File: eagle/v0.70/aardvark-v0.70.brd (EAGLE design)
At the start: 25.4 x 76.2 mm, 22 parts, among them IC1 REG1117, X1 MINI-USB-32005-201

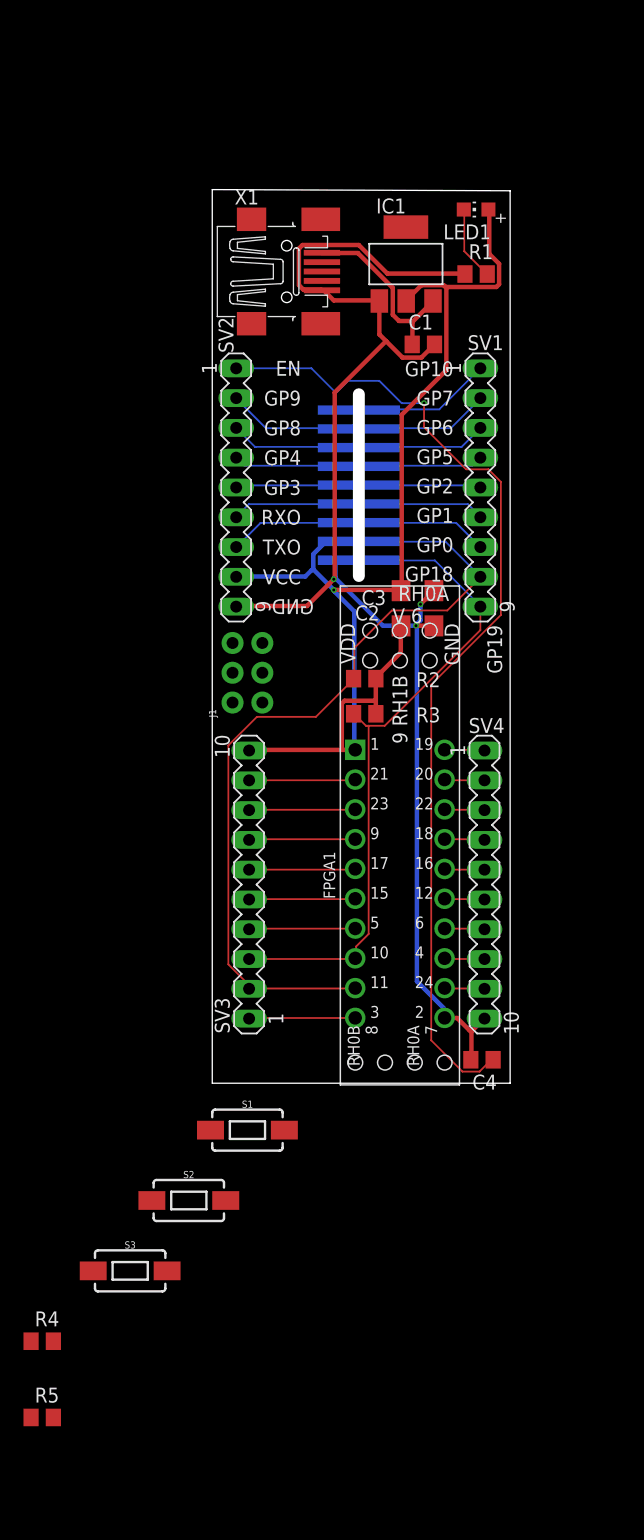
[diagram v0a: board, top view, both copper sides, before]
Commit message: fixed spelling error and mirror image GND designator
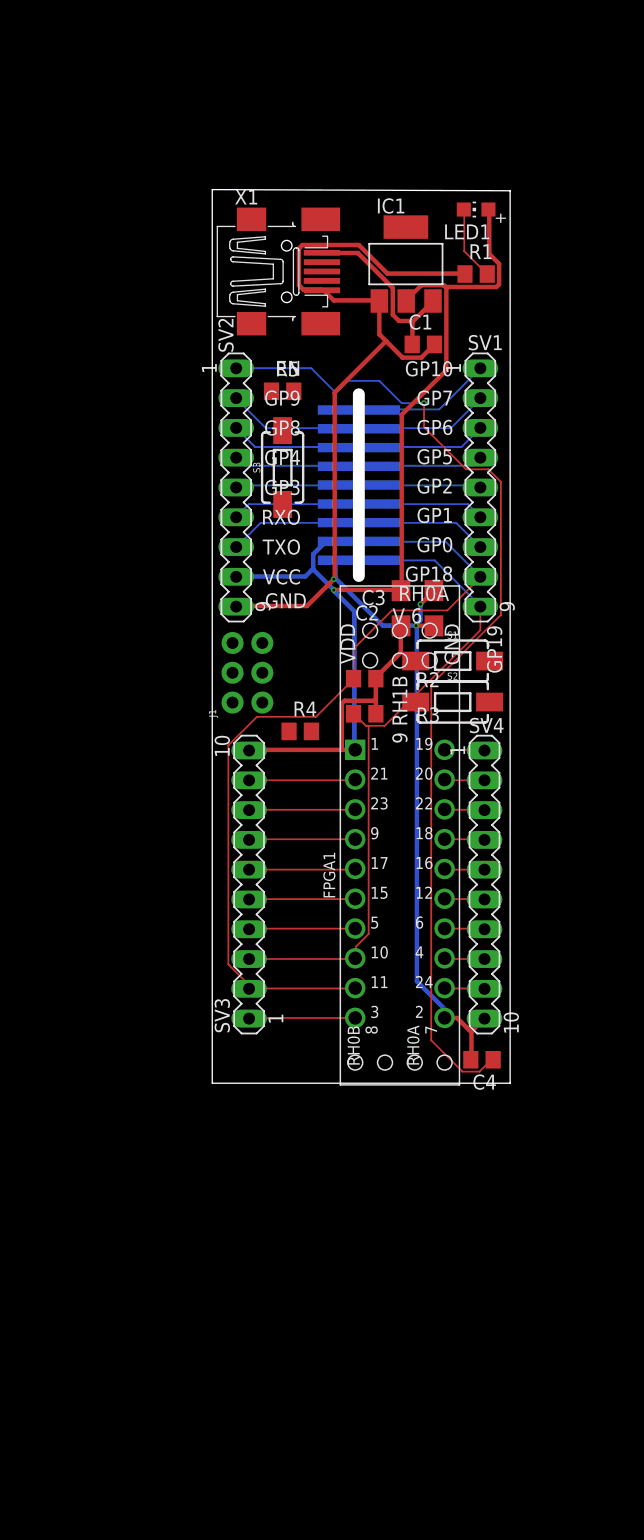
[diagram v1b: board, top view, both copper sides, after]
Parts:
- moved R5 89.9 mm to (6.00, 59.0)
- moved S3 69.7 mm to (6.00, 52.5), turned to 90 degrees
- moved R4 56.5 mm to (7.50, 30.0)
- moved S2 48.1 mm to (20.5, 32.5)
- moved S1 43.7 mm to (20.5, 36.0)
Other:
- board text added: "TriEmbed Community Project Aardvarck 0.70 ESP32-C3 + SLG47004V-DIP"
- board text removed: "TriEmbed Community Project Aardvack 0.70 ESP32-C3 + SLG47004V-DIP"

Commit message: board update: incomplete placement and routing
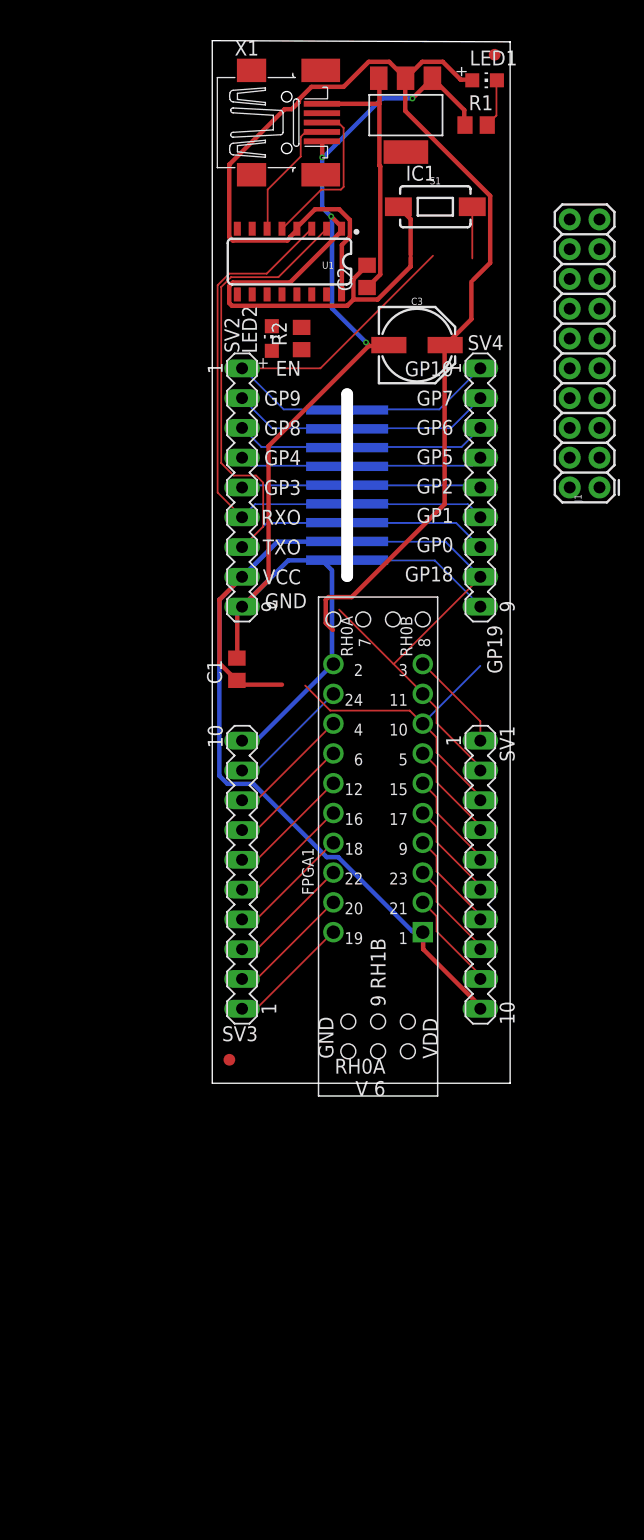
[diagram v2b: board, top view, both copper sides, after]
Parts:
- removed C4: 4.7uF, rcl:C0805
- removed R3: 10K, rcl:R0805
- removed R4, R5: 4.7k, rcl:R0805
- removed S2: BOOT, apexprotofactory:TACTILE_SWITCH_SMD_6.0X3.5MM
- removed S3: VERBOSE, apexprotofactory:TACTILE_SWITCH_SMD_6.0X3.5MM
- removed U$2: UNTITLED_ESP32C3, aardvark-v0.01:UNTITLED_ESP32-C3-01M
- added FD1, FD2: FIDUCIAL1X2, apexprotofactory:FIDUCIAL-1X2
- added LED2: (no value), adafruit:CHIP-LED0805
- added MOD1: (no value), aithinker-C3-M1:ESPRESSIF_ESP32-C3-01M
- added U1: CH340C, SparkFun-IC-Comms:SO016
- C1: value 10uF -> 100nF
- C2: value 68uF -> 10uF; device rcl:C1206 -> rcl:C0805
- C3: value 68uF -> 100uF; device rcl:C1206 -> SparkFun-Capacitors:PANASONIC_D
- FPGA1: value SLG47004V-DIP -> (none); device 22020117-1206PM-SLG47004V-DIP:SLG47004V-DIP -> SLG47004V-DIP:SLG47004V-DIP
- IC1: value REG1117 -> LM1117-3.3
- J1: device SparkFun-Connectors:2X3-NS -> SparkFun-Connectors:2X10
- R2: value 10K -> 510
- S1: value ENABLE -> RESET; device apexprotofactory:TACTILE_SWITCH_SMD_6.0X3.5MM -> SparkFun-Switches:TACTILE_SWITCH_SMD_6.0X3.5MM
- SV1: device con-lstb:MA09-1 -> con-lstb:MA10-1
- SV4: device con-lstb:MA10-1 -> con-lstb:MA09-1
- moved S1 38.8 mm to (19.0, 74.7)
- moved J1 33.9 mm to (33.0, 50.8)
- moved SV4 33.9 mm to (22.9, 50.8)
- moved SV1 33.0 mm to (22.9, 17.8)
- moved C1 31.9 mm to (2.10, 35.3), turned to 90 degrees
- moved C2 30.1 mm to (13.2, 68.8), turned to 90 degrees
- moved R2 29.5 mm to (7.62, 63.5), turned to 90 degrees
- moved C3 20.9 mm to (17.5, 62.9)
- moved IC1 12.7 mm to (16.5, 82.5), turned to 180 degrees
- moved R1 12.7 mm to (22.5, 81.7)
- moved X1 12.7 mm to (6.35, 81.9)
- moved LED1 11.0 mm to (23.2, 85.5), turned to 270 degrees
- moved FPGA1 2.09 mm to (14.1, 18.0), turned to 90 degrees
- moved SV3 1.03 mm to (2.54, 17.8)
- moved SV2 0.50 mm to (2.54, 50.8)
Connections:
- removed net DP4: SV2.4, U$2.PIN4
- removed net GP0: SV1.7, U$2.PIN12
- removed net GP1: SV1.6, U$2.PIN13
- removed net RXO: SV2.6, U$2.PIN6
- new net DTR: U1.13
- new net GP18: MOD1.PIN11, SV4.8
- new net GP19: MOD1.PIN10, SV4.9
- new net GP4: MOD1.PIN4, SV2.4
- new net N$1: LED2.C, R2.2
- new net RTS: U1.14
- new net RXI: MOD1.PIN6, SV2.6, U1.3
- new net UD+: U1.5, X1.3
- new net UD-: U1.6, X1.4
- net EN: now also MOD1.PIN1; no longer C4.1, U$2.PIN1
- net GND: now also C3.-, MOD1.PIN9, R2.1, SV3.10, U1.1; no longer C3.2, C4.2, S2.1, S3.1, SV4.10, U$2.PIN9
- net GP10: now also MOD1.PIN18, SV4.1; no longer SV1.1, U$2.PIN18
- net GP2: now also LED2.A, MOD1.PIN14, SV4.5; no longer SV1.5, U$2.PIN14
- net GP3: now also MOD1.PIN5; no longer U$2.PIN5
- net GP5: now also MOD1.PIN15, SV4.4; no longer SV1.4, U$2.PIN15
- net GP6: now also MOD1.PIN16, SV4.3; no longer SV1.3, U$2.PIN16
- net GP7: now also MOD1.PIN17, SV4.2; no longer SV1.2, U$2.PIN17
- net GP8: now also MOD1.PIN3; no longer R5.2, S3.2, U$2.PIN3
- net GP9: now also MOD1.PIN2; no longer R4.2, S2.2, U$2.PIN2
- net GPI(PIN21): now also SV1.9; no longer SV3.9
- net GPIO(PIN12): now also SV3.6; no longer SV4.6
- net GPIO(PIN15): now also SV1.5; no longer SV3.5
- net GPIO(PIN16): now also SV3.5; no longer SV4.5
- net GPIO(PIN17): now also SV1.6; no longer SV3.6
- net GPIO(PIN18): now also SV3.4; no longer SV4.4
- net GPIO(PIN19): now also SV3.1; no longer SV4.1
- net GPIO(PIN20): now also SV3.2; no longer SV4.2
- net OA0+(PIN4): now also SV3.8; no longer SV4.8
- net OA0-(PIN3): now also SV1.1; no longer SV3.1
- net OA0_OUT(PIN5): now also SV1.4; no longer SV3.4
- net OA1+(PIN23): now also SV1.8; no longer SV3.8
- net OA1-(PIN24): now also SV3.9; no longer SV4.9
- net OA1_OUT(PIN22): now also SV3.3; no longer SV4.3
- net RH0A(PIN6): now also SV3.7; no longer SV4.7
- net RH1B(PIN9): now also SV1.7; no longer SV3.7
- net SCL: now also MOD1.PIN12, SV1.3, SV4.7; no longer R3.1, SV1.9, SV3.3, U$2.PIN10
- net SDA: now also MOD1.PIN13, SV1.2, SV4.6; no longer R2.1, SV1.8, SV3.2, U$2.PIN11
- net TXO: now also MOD1.PIN7, U1.2; no longer U$2.PIN7
- net USBV: now also C2.1; no longer C1.1
- net VCC: now also C1.1, C3.+, MOD1.PIN8, SV1.10, U1.16, U1.4; no longer C2.1, C3.1, R2.2, R3.2, R4.1, R5.1, SV3.10, U$2.PIN8
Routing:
- net VCC: track 100.4 -> 180.0 mm, vias 1 -> 0
- net EN: track 87.0 -> 33.1 mm, vias 1 -> 0
- net RXI: track 0.00 -> 38.1 mm
- net TXO: track 9.32 -> 44.4 mm
- net SDA: track 69.2 -> 39.0 mm
- net SCL: track 56.0 -> 37.1 mm
- net GND: track 122.7 -> 138.0 mm, vias 3 -> 4
- net UD+: track 0.00 -> 13.8 mm
- net GP19: track 0.00 -> 11.0 mm
- net UD-: track 0.00 -> 11.0 mm
- net GP18: track 0.00 -> 10.6 mm
- net GP0: track 9.22 -> 0.00 mm
- net RXO: track 8.94 -> 0.00 mm
- net GP1: track 8.86 -> 0.00 mm
- net DP4: track 8.76 -> 0.00 mm
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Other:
- board size 25.4 x 76.2 mm -> 25.4 x 88.9 mm

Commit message: Fix C3 module footprint, shift pin outside SLG footprint, update notes
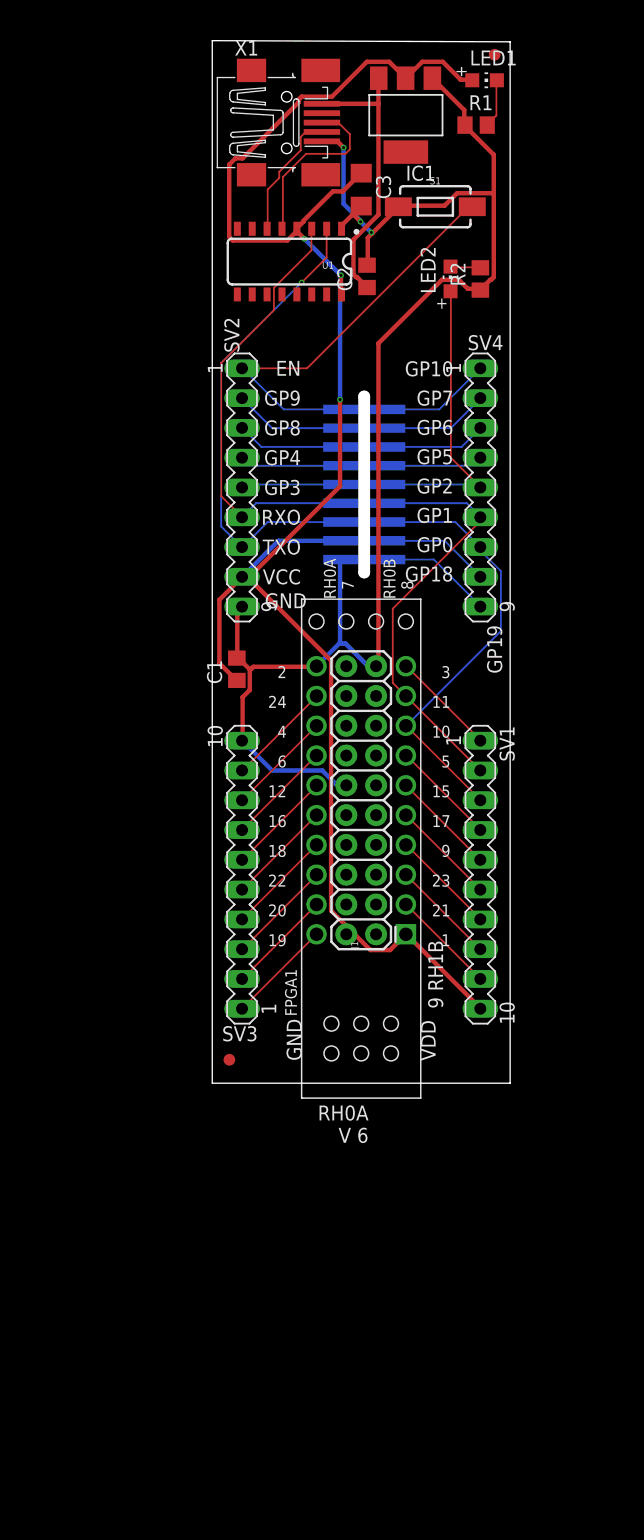
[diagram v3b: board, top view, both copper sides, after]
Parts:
- C3: value 100uF -> (none); device SparkFun-Capacitors:PANASONIC_D -> rcl:C1206
- moved J1 42.6 mm to (14.0, 12.7)
- moved LED2 16.1 mm to (20.3, 68.6)
- moved R2 16.1 mm to (22.9, 68.6)
- moved C3 14.1 mm to (12.7, 76.2), turned to 270 degrees
- moved MOD1 1.46 mm to (13.0, 51.1)
- moved FPGA1 1.45 mm to (12.7, 17.8)
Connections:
- net GND: now also C3.2, J1.12, J1.19; no longer C3.-
- net VCC: now also C3.1, J1.2; no longer C3.+
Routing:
- net VCC: track 180.0 -> 152.7 mm, vias 0 -> 3
- net GP2: track 9.45 -> 25.8 mm
- net GND: track 138.0 -> 130.8 mm, vias 4 -> 3
- net TXO: track 44.4 -> 40.9 mm, vias 0 -> 1
- net SDA: track 39.0 -> 36.2 mm
- net N$1: track 0.00 -> 2.62 mm
- net EN: track 33.1 -> 35.2 mm
- net GPIO(PIN18): track 10.5 -> 8.98 mm
- net GPIO(PIN19): track 10.5 -> 8.98 mm
- net RH0A(PIN6): track 10.5 -> 8.98 mm
- net GP3: track 7.03 -> 8.51 mm
- net GP10: track 10.8 -> 9.36 mm
- net GP7: track 10.5 -> 9.00 mm
- net GP6: track 10.1 -> 8.59 mm
- net GP5: track 9.66 -> 8.19 mm
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
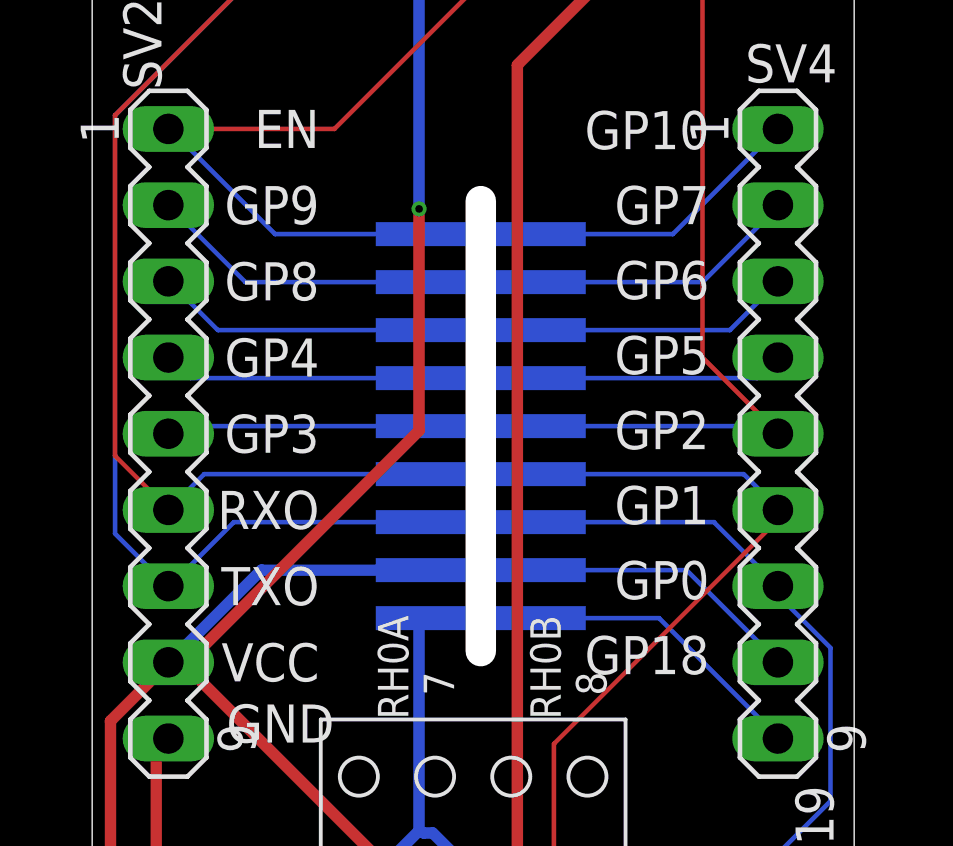
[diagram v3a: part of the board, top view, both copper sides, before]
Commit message: swap C3 board in that really has slot narrowed
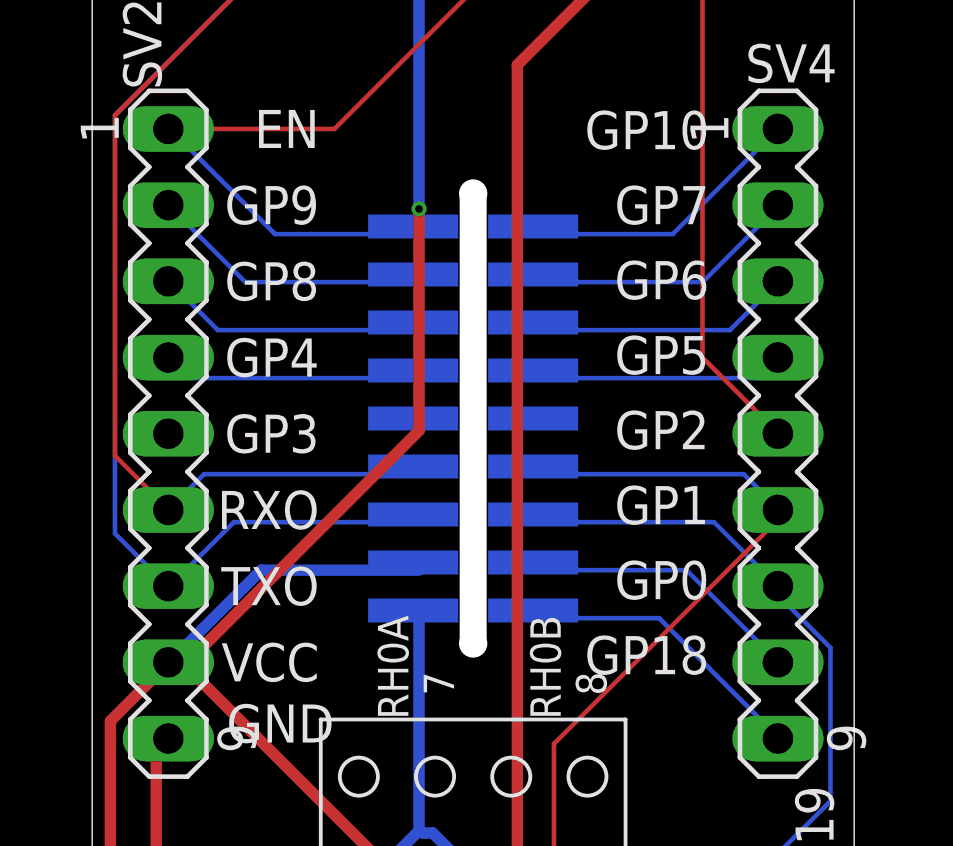
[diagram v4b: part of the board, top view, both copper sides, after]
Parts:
- moved MOD1 0.36 mm to (12.7, 51.3)
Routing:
- net GP3: track 8.51 -> 0.38 mm
- net GP2: track 25.8 -> 18.1 mm

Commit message: added right angle header site for outboard I2C programming
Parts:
- added SV5: (no value), con-lstb:MA04-1
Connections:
- net GND: now also SV5.1
- net SCL: now also SV5.3
- net SDA: now also SV5.4
- net VCC: now also SV5.2
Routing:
- net GND: track 130.8 -> 165.0 mm
- net SDA: track 36.1 -> 65.9 mm
- net SCL: track 37.1 -> 65.6 mm
- net GP2: track 18.1 -> 26.2 mm
- net GP3: track 0.38 -> 8.36 mm
- net VCC: track 152.7 -> 159.8 mm

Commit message: 0.70 release candidate
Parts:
- removed X1: MINI-USB-32005-201, con-cypressindustries:32005-201
- added DIALOG-PGM: (no value), SparkFun-Connectors:2X10
- added LOGO1: OSHW-LOGOMINI, SparkFun-Aesthetics:OSHW-LOGO-MINI
- C1: value 100nF -> 10uF
- C2: value 10uF -> 100uF; device rcl:C0805 -> SparkFun-Capacitors:PANASONIC_D
- C3: value (none) -> 4.7uF; device rcl:C1206 -> rcl:C0805
- FPGA1: value (none) -> SLG47004V-DIP
- J1: value (none) -> USB_MINI-B_SMT; device SparkFun-Connectors:2X10 -> SparkFun-Connectors:USB-MINIB
- LED1, LED2: device adafruit:CHIP-LED0805 -> led:CHIP-LED0805
- MOD1: value (none) -> ESP32-C3-M1; device aithinker-C3-M1:ESPRESSIF_ESP32-C3-01M -> aithinker-C3-M1:AITHINKER-C3-M1
- SV2: device con-lstb:MA09-1 -> con-lstb:MA04-1
- SV3: device con-lstb:MA10-1 -> con-lstb:MA09-1
- SV4: device con-lstb:MA09-1 -> con-lstb:MA10-1
- SV5: device con-lstb:MA04-1 -> con-lstb:MA09-1
- moved J1 70.7 mm to (4.70, 82.8), turned to 0 degrees
- moved SV5 48.6 mm to (22.9, 50.8), turned to 270 degrees
- moved C1 43.9 mm to (12.3, 78.0), turned to 180 degrees
- moved SV4 37.7 mm to (2.54, 19.1), turned to 90 degrees
- moved SV3 33.0 mm to (2.54, 50.8), turned to 270 degrees
- moved C2 16.0 mm to (20.7, 82.9)
- moved LED1 15.7 mm to (13.7, 73.0)
- moved R1 14.8 mm to (13.5, 70.0)
- moved SV2 13.5 mm to (5.17, 64.1), turned to 0 degrees
- moved C3 10.4 mm to (12.4, 65.8)
- moved LED2 6.13 mm to (15.5, 64.8)
- moved R2 5.50 mm to (18.7, 65.0), turned to 270 degrees
- moved IC1 3.55 mm to (13.3, 84.0), turned to 0 degrees
- moved U1 3.21 mm to (5.30, 73.0), turned to 0 degrees
- moved S1 2.50 mm to (20.4, 72.7), turned to 270 degrees
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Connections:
- removed net DTR: U1.13
- removed net RTS: U1.14
- removed net USBV: C2.1, IC1.3, X1.1
- new net VBUS: C1.1, IC1.3, J1.VBUS
- net EN: now also C3.1, SV3.1, U1.14; no longer SV2.1
- net GND: now also C2.-, DIALOG-PGM.12, DIALOG-PGM.19, J1.GND, SV2.1, SV3.9, SV4.10; no longer C2.2, J1.12, J1.19, SV2.9, SV3.10, SV5.1, X1.5
- net GP10: now also SV5.1; no longer SV4.1
- net GP18: now also SV5.8; no longer SV4.8
- net GP19: now also SV5.9; no longer SV4.9
- net GP2: now also SV5.5; no longer SV4.5
- net GP3: now also SV3.5; no longer SV2.5
- net GP4: now also SV3.4; no longer SV2.4
- net GP5: now also SV5.4; no longer SV4.4
- net GP6: now also SV5.3; no longer SV4.3
- net GP7: now also SV5.2; no longer SV4.2
- net GP8: now also SV3.3; no longer SV2.3
- net GP9: now also SV3.2, U1.13; no longer SV2.2
- net GPIO(PIN12): now also SV4.6; no longer SV3.6
- net GPIO(PIN16): now also SV4.5; no longer SV3.5
- net GPIO(PIN18): now also SV4.4; no longer SV3.4
- net GPIO(PIN19): now also SV4.1; no longer SV3.1
- net GPIO(PIN20): now also SV4.2; no longer SV3.2
- net OA0+(PIN4): now also SV4.8; no longer SV3.8
- net OA1-(PIN24): now also SV4.9; no longer SV3.9
- net OA1_OUT(PIN22): now also SV4.3; no longer SV3.3
- net RH0A(PIN6): now also SV4.7; no longer SV3.7
- net RXI: now also SV3.6; no longer SV2.6
- net SCL: now also DIALOG-PGM.8, SV2.3, SV5.7; no longer SV4.7, SV5.3
- net SDA: now also DIALOG-PGM.9, SV2.4, SV5.6; no longer SV4.6, SV5.4
- net TXO: now also SV3.7; no longer SV2.7
- net UD+: now also J1.D+; no longer X1.3
- net UD-: now also J1.D-; no longer X1.4
- net VCC: now also C2.+, DIALOG-PGM.2, SV2.2, SV3.8; no longer C1.1, C3.1, J1.2, SV2.8, SV5.2
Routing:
- net EN: track 34.9 -> 85.6 mm, vias 0 -> 1
- net GND: track 165.0 -> 138.2 mm, vias 3 -> 1
- net VCC: track 159.8 -> 134.7 mm, vias 3 -> 2
- net USBV: track 24.1 -> 0.00 mm
- net GP9: track 9.12 -> 28.2 mm, vias 0 -> 2
- net VBUS: track 0.00 -> 12.6 mm, vias 0 -> 2
- net SDA: track 65.9 -> 77.4 mm
- net SCL: track 65.6 -> 75.5 mm
- net TXO: track 40.8 -> 34.5 mm
- net RXI: track 37.3 -> 31.6 mm, vias 0 -> 2
- net UD-: track 11.0 -> 15.3 mm
- net GP2: track 26.2 -> 24.7 mm
- net N$1: track 2.62 -> 3.93 mm
- net N$3: track 4.16 -> 3.15 mm
- net UD+: track 15.2 -> 14.2 mm
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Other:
- board text added: "SCL"
- board text added: "SDA"
- board text added: "TriEmbed Community Aardvarck 0.70 CC BY-SA 2.0 ESP32-C3 + SLG47004V-DIP"
- board text removed: "TriEmbed Community Project Aardvarck 0.70 ESP32-C3 + SLG47004V-DIP"
